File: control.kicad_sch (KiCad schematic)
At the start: 15 parts, among them U16001 OPA2810

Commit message: move symbols to project specific library
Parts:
- C16001, C16002, C16003, C16004, C16005, C16006: symbol Device:C -> pss:C
- R16001, R16002, R16003, R16004, R16005, R16006, R16007, R16008: symbol Device:R -> pss:R
- U16001: symbol Device:Opamp_Dual -> pss:Opamp_Dual
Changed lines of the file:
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@@
 	)
 	(symbol
-		(lib_id "Device:R")
+		(lib_id "pss:R")
 		(at 111.76 76.2 90)
 		(unit 1)
@@
 	)
 	(symbol
-		(lib_id "power:GND")
+		(lib_id "pss:GND")
 		(at 104.14 187.96 0)
 		(unit 1)
@@
 	)
 	(symbol
-		(lib_id "power:-5V")
+		(lib_id "pss:-5V")
 		(at 88.9 177.8 180)
 		(unit 1)
@@
 	)
 	(symbol
-		(lib_id "Device:C")
+		(lib_id "pss:C")
 		(at 119.38 181.61 0)
 		(unit 1)
@@
 	)
 	(symbol
-		(lib_id "Device:C")
+		(lib_id "pss:C")
 		(at 104.14 181.61 0)
 		(unit 1)
@@
 	)
 	(symbol
-		(lib_id "power:+10V")
+		(lib_id "pss:+10V")
 		(at 88.9 148.59 0)
 		(unit 1)
@@
 	)
 	(symbol
-		(lib_id "Device:R")
+		(lib_id "pss:R")
 		(at 171.45 113.03 180)
 		(unit 1)
@@
 	)
 	(symbol
-		(lib_id "Device:Opamp_Dual")
+		(lib_id "pss:Opamp_Dual")
 		(at 91.44 165.1 0)
 		(unit 3)
@@
 	)
 	(symbol
-		(lib_id "Device:R")
+		(lib_id "pss:R")
 		(at 111.76 104.14 90)
 		(unit 1)
@@
 	)
 	(symbol
-		(lib_id "Device:R")
+		(lib_id "pss:R")
 		(at 133.35 76.2 90)
 		(unit 1)
@@
 	)
 	(symbol
-		(lib_id "Device:C")
+		(lib_id "pss:C")
 		(at 196.85 78.74 90)
 		(unit 1)
@@
 	)
 	(symbol
-		(lib_id "power:GND")
+		(lib_id "pss:GND")
 		(at 203.2 91.44 0)
 		(unit 1)
@@
 	)
 	(symbol
-		(lib_id "Device:C")
+		(lib_id "pss:C")
 		(at 203.2 85.09 0)
 		(unit 1)
@@
 	)
 	(symbol
-		(lib_id "power:GND")
+		(lib_id "pss:GND")
 		(at 119.38 187.96 0)
 		(unit 1)
@@
 	)
 	(symbol
-		(lib_id "Device:R")
+		(lib_id "pss:R")
 		(at 184.15 78.74 270)
 		(unit 1)
@@
 	)
 	(symbol
-		(lib_id "power:GND")
+		(lib_id "pss:GND")
 		(at 171.45 119.38 0)
 		(unit 1)
@@
 	)
 	(symbol
-		(lib_id "power:GND")
+		(lib_id "pss:GND")
 		(at 120.65 116.84 0)
 		(unit 1)
@@
 	)
 	(symbol
-		(lib_id "Device:Opamp_Dual")
+		(lib_id "pss:Opamp_Dual")
 		(at 132.08 101.6 0)
 		(unit 1)
@@
 	)
 	(symbol
-		(lib_id "power:GND")
+		(lib_id "pss:GND")
 		(at 119.38 165.1 0)
 		(unit 1)
@@
 	)
 	(symbol
-		(lib_id "Device:Opamp_Dual")
+		(lib_id "pss:Opamp_Dual")
 		(at 184.15 104.14 0)
 		(mirror x)
@@
 	)
 	(symbol
-		(lib_id "Device:R")
+		(lib_id "pss:R")
 		(at 120.65 110.49 180)
 		(unit 1)
@@
 	)
 	(symbol
-		(lib_id "Device:C")
+		(lib_id "pss:C")
 		(at 119.38 158.75 0)
 		(unit 1)
@@
 	)
 	(symbol
-		(lib_id "power:GND")
+		(lib_id "pss:GND")
 		(at 104.14 165.1 0)
 		(unit 1)
@@
 	)
 	(symbol
-		(lib_id "Device:R")
+		(lib_id "pss:R")
 		(at 158.75 101.6 270)
 		(unit 1)
@@
 	)
 	(symbol
-		(lib_id "Device:C")
+		(lib_id "pss:C")
 		(at 104.14 158.75 0)
 		(unit 1)
@@
 	)
 	(symbol
-		(lib_id "Device:R")
+		(lib_id "pss:R")
 		(at 209.55 78.74 270)
 		(unit 1)

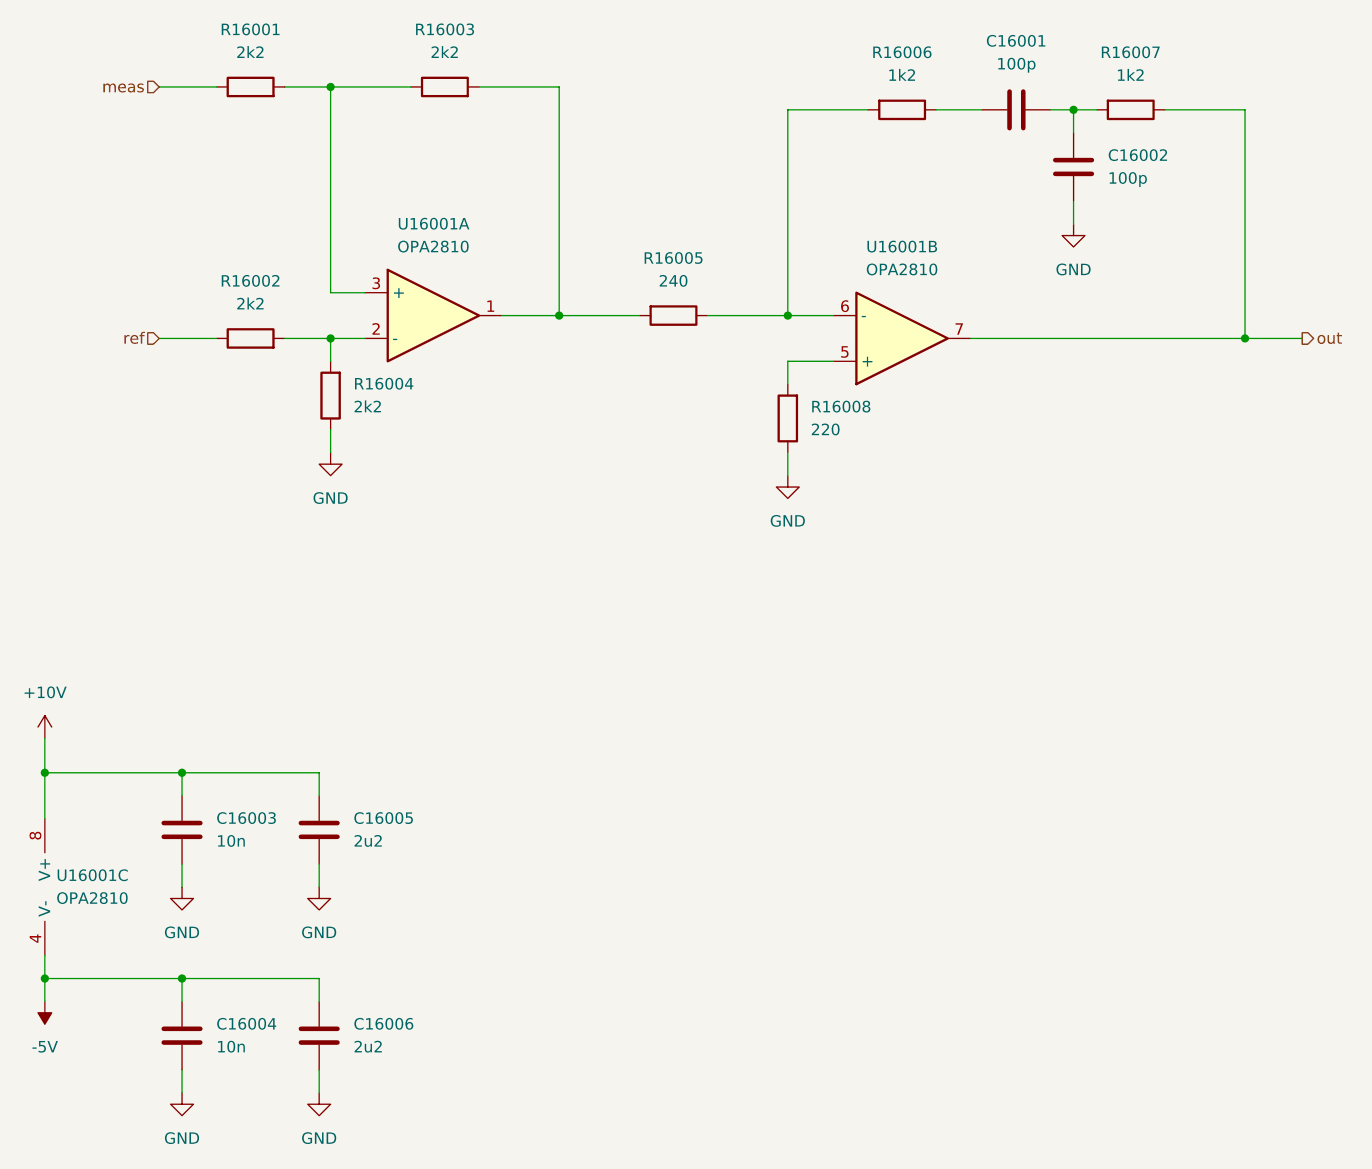
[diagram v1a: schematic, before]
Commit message: refactor schematic hirarchy
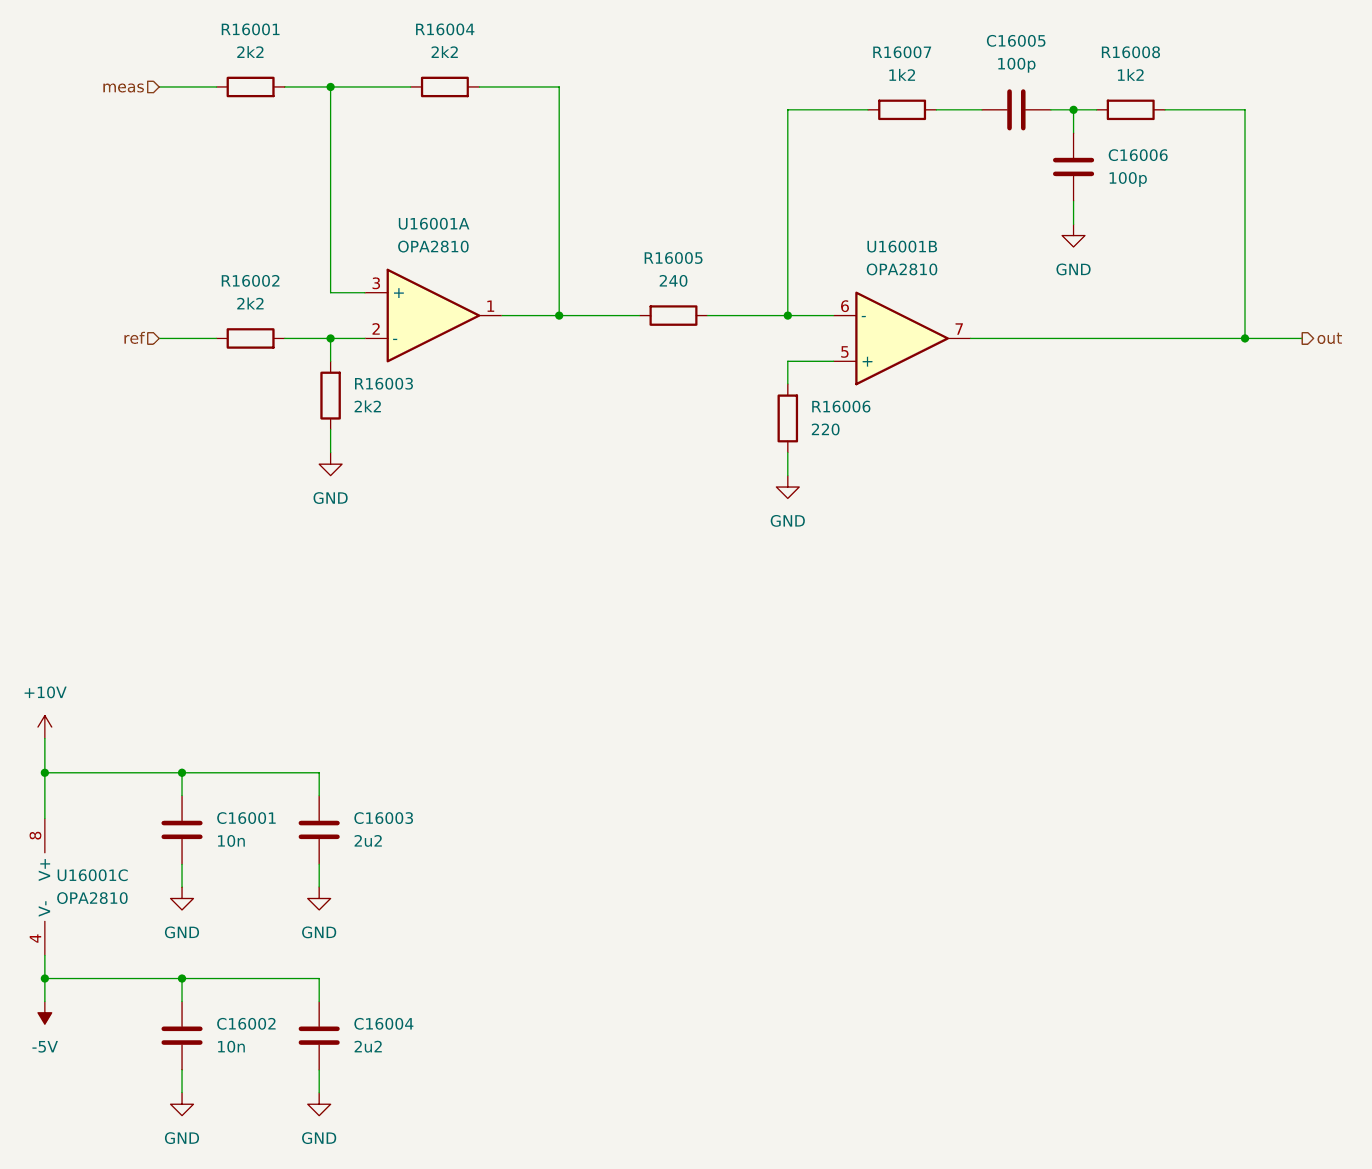
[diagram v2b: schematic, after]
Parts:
- renumbered C16003 to C16001, C16004 to C16002, C16005 to C16003, C16006 to C16004, C16001 to C16005, C16002 to C16006, R16004 to R16003, R16003 to R16004, R16008 to R16006, R16006 to R16007, R16007 to R16008
